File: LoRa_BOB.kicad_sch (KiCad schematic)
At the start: 14 parts, among them U1 1597-1488-ND, U2 XC6210B332MR-G, U3 74HC4050D

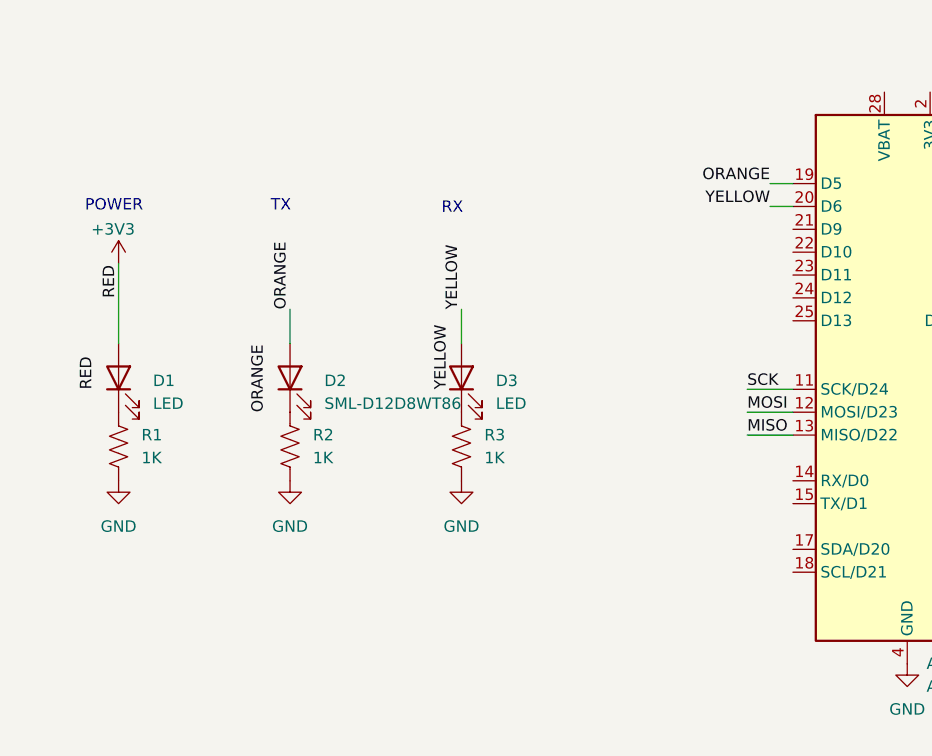
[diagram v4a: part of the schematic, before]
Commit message: better LEDs
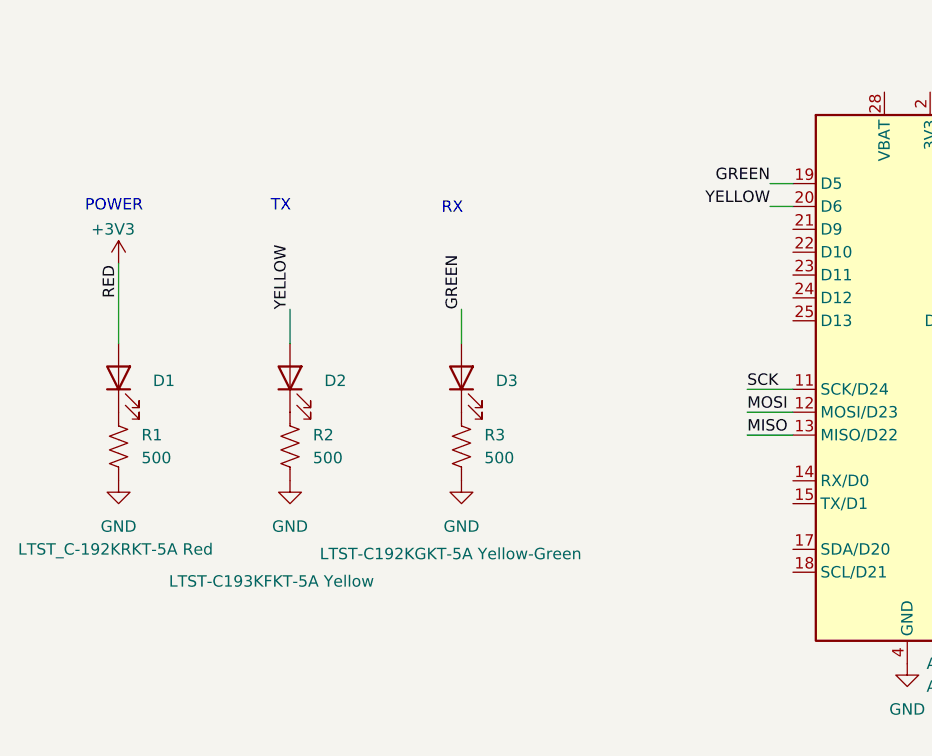
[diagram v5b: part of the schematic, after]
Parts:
- D1: value LED -> LTST_C-192KRKT-5A Red
- D2: value SML-D12D8WT86 -> LTST-C193KFKT-5A Yellow
- D3: value LED -> LTST-C192KGKT-5A Yellow-Green
- R1, R2, R3: value 1K -> 500
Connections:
- net YELLOW: now also D2.2 (A); no longer D3.2 (A)
- net ORANGE renamed GREEN
- net GREEN: now also D3.2 (A); no longer D2.2 (A)
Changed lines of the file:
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@@
 		)
 	)
-	(label "RED"
-		(at 81.28 124.46 90)
-		(effects
-			(font
-				(size 1.27 1.27)
-			)
-			(justify left bottom)
-		)
-	)
-	(label "YELLOW"
+	(label "GREEN"
 		(at 121.92 115.57 90)
 		(effects
@@
 		)
 	)
-	(label "ORANGE"
+	(label "YELLOW"
 		(at 102.87 115.57 90)
 		(effects
@@
 		)
 	)
-	(label "ORANGE"
+	(label "GREEN"
 		(at 156.21 101.6 180)
 		(effects
@@
 		)
 	)
-	(label "YELLOW"
-		(at 120.65 124.46 90)
-		(effects
-			(font
-				(size 1.27 1.27)
-			)
-			(justify left bottom)
-		)
-	)
 	(label "MISO"
 		(at 323.85 166.37 0)
@@
 	(label "SCK_3V"
 		(at 240.03 129.54 0)
-		(effects
-			(font
-				(size 1.27 1.27)
-			)
-			(justify left bottom)
-		)
-	)
-	(label "ORANGE"
-		(at 100.33 127 90)
 		(effects
 			(font
@@
 			)
 		)
-		(property "Value" "1K"
+		(property "Value" "500"
 			(at 105.41 132.0799 0)
 			(effects
@@
 		(on_board yes)
 		(dnp no)
-		(fields_autoplaced yes)
 		(property "Reference" "D3"
 			(at 125.73 123.5074 90)
@@
 			)
 		)
-		(property "Value" "LED"
-			(at 125.73 126.0474 90)
+		(property "Value" "LTST-C192KGKT-5A Yellow-Green"
+			(at 106.172 142.748 90)
 			(effects
 				(font
@@
 			)
 		)
-		(property "Datasheet" "~"
+		(property "Datasheet" "https://www.mouser.com/catalog/specsheets/LTST-C193_Series.pdf"
 			(at 121.92 123.19 0)
 			(effects
@@
 		(on_board yes)
 		(dnp no)
-		(fields_autoplaced yes)
 		(property "Reference" "D1"
 			(at 87.63 123.5074 90)
@@
 			)
 		)
-		(property "Value" "LED"
-			(at 87.63 126.0474 90)
+		(property "Value" "LTST_C-192KRKT-5A Red"
+			(at 72.644 142.24 90)
 			(effects
 				(font
@@
 			)
 		)
-		(property "Datasheet" "~"
+		(property "Datasheet" "https://www.mouser.com/catalog/specsheets/LTST-C193_Series.pdf"
 			(at 83.82 123.19 0)
 			(effects
@@
 		(on_board yes)
 		(dnp no)
-		(fields_autoplaced yes)
 		(property "Reference" "D2"
 			(at 106.68 123.5074 90)
@@
 			)
 		)
-		(property "Value" "SML-D12D8WT86"
-			(at 106.68 126.0474 90)
+		(property "Value" "LTST-C193KFKT-5A Yellow"
+			(at 89.408 145.796 90)
 			(effects
 				(font
@@
 			)
 		)
-		(property "Datasheet" "https://www.rohm.com/datasheet?p=SML-D12D8W&dist=Digi-key&media=referral&source=digi-key.com&campaign=Digi-key"
+		(property "Datasheet" "https://www.mouser.com/catalog/specsheets/LTST-C193_Series.pdf"
 			(at 102.87 123.19 0)
 			(effects
@@
 			)
 		)
-		(property "Value" "1K"
+		(property "Value" "500"
 			(at 86.36 132.0799 0)
 			(effects
@@
 			)
 		)
-		(property "Value" "1K"
+		(property "Value" "500"
 			(at 124.46 132.0799 0)
 			(effects

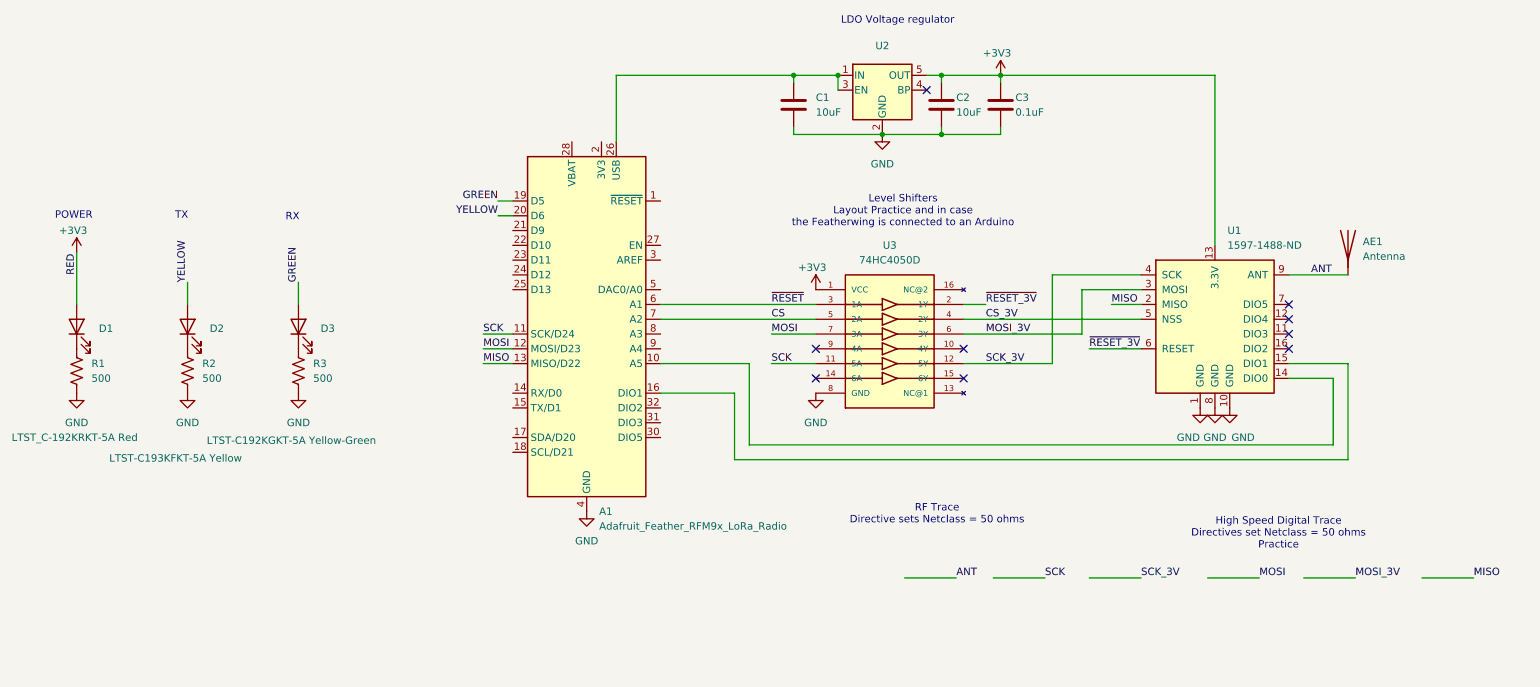
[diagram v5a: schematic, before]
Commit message: Power Flags
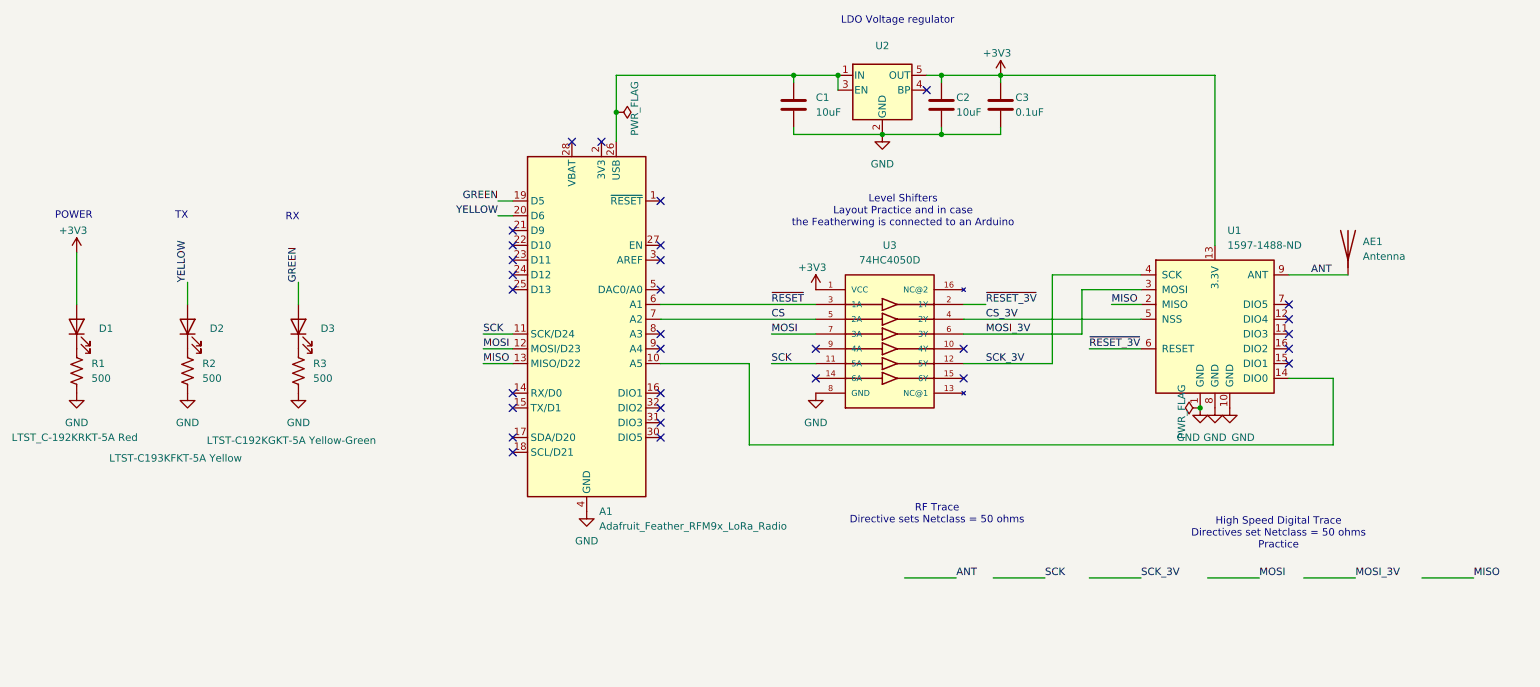
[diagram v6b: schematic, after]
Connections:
- net at A1.16 (DIO1): no longer U1.15 (DIO1)
- no-connect marks 9 -> 31
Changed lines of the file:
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@@
+	)
+	(junction
+		(at 176.53 86.36)
+		(diameter 0)
+		(color 0 0 0 0)
 	)
 	(junction
@@
 		(color 0 0 0 0)
 	)
+	(junction
+		(at 276.86 137.16)
+		(diameter 0)
+		(color 0 0 0 0)
+	)
+	(no_connect
+		(at 184.15 101.6)
+	)
 	(no_connect
 		(at 292.1 127)
 	)
 	(no_connect
+		(at 184.15 111.76)
+	)
+	(no_connect
+		(at 158.75 144.78)
+	)
+	(no_connect
+		(at 184.15 134.62)
+	)
+	(no_connect
+		(at 184.15 139.7)
+	)
+	(no_connect
 		(at 292.1 124.46)
 	)
@@
 	)
 	(no_connect
+		(at 158.75 111.76)
+	)
+	(no_connect
+		(at 168.91 91.44)
+	)
+	(no_connect
+		(at 173.99 91.44)
+	)
+	(no_connect
+		(at 184.15 116.84)
+	)
+	(no_connect
 		(at 229.87 82.55)
 	)
 	(no_connect
+		(at 158.75 114.3)
+	)
+	(no_connect
+		(at 158.75 137.16)
+	)
+	(no_connect
+		(at 158.75 142.24)
+	)
+	(no_connect
+		(at 158.75 116.84)
+	)
+	(no_connect
+		(at 184.15 127)
+	)
+	(no_connect
+		(at 184.15 142.24)
+	)
+	(no_connect
+		(at 158.75 106.68)
+	)
+	(no_connect
+		(at 184.15 124.46)
+	)
+	(no_connect
+		(at 184.15 137.16)
+	)
+	(no_connect
 		(at 236.22 132.08)
 	)
 	(no_connect
+		(at 158.75 134.62)
+	)
+	(no_connect
+		(at 158.75 109.22)
+	)
+	(no_connect
 		(at 210.82 132.08)
 	)
 	(no_connect
+		(at 292.1 129.54)
+	)
+	(no_connect
+		(at 184.15 109.22)
+	)
+	(no_connect
 		(at 236.22 127)
 	)
@@
 	(wire
 		(pts
+			(xy 176.53 86.36) (xy 176.53 80.01)
+		)
+		(stroke
+			(width 0)
+			(type default)
+		)
+	)
+	(wire
+		(pts
 			(xy 256.54 116.84) (xy 266.7 116.84)
 		)
@@
 	(wire
 		(pts
-			(xy 302.26 129.54) (xy 302.26 146.05)
-		)
-		(stroke
-			(width 0)
-			(type default)
-		)
-	)
-	(wire
-		(pts
 			(xy 232.41 80.01) (xy 232.41 81.28)
 		)
@@
 	(wire
 		(pts
-			(xy 196.85 146.05) (xy 302.26 146.05)
-		)
-		(stroke
-			(width 0)
-			(type default)
-		)
-	)
-	(wire
-		(pts
 			(xy 236.22 124.46) (xy 256.54 124.46)
 		)
@@
 	(wire
 		(pts
-			(xy 292.1 129.54) (xy 302.26 129.54)
-		)
-		(stroke
-			(width 0)
-			(type default)
-		)
-	)
-	(wire
-		(pts
 			(xy 153.67 129.54) (xy 158.75 129.54)
 		)
@@
 	(wire
 		(pts
-			(xy 176.53 91.44) (xy 176.53 80.01)
+			(xy 176.53 91.44) (xy 176.53 86.36)
 		)
 		(stroke
@@
 	(wire
 		(pts
-			(xy 184.15 134.62) (xy 196.85 134.62)
-		)
-		(stroke
-			(width 0)
-			(type default)
-		)
-	)
-	(wire
-		(pts
 			(xy 242.57 80.01) (xy 242.57 81.28)
-		)
-		(stroke
-			(width 0)
-			(type default)
-		)
-	)
-	(wire
-		(pts
-			(xy 196.85 134.62) (xy 196.85 146.05)
 		)
 		(stroke
@@
 		)
 	)
-	(label "RED"
-		(at 83.82 114.3 90)
-		(effects
-			(font
-				(size 1.27 1.27)
-			)
-			(justify left bottom)
-		)
-	)
 	(label "SCK_3V"
 		(at 266.7 166.37 0)
@@
 	)
 	(symbol
+		(lib_id "power:PWR_FLAG")
+		(at 176.53 86.36 270)
+		(unit 1)
+		(exclude_from_sim no)
+		(in_bom yes)
+		(on_board yes)
+		(dnp no)
+		(property "Reference" "#FLG02"
+			(at 178.435 86.36 0)
+			(effects
+				(font
+					(size 1.27 1.27)
+				)
+				(hide yes)
+			)
+		)
+		(property "Value" "PWR_FLAG"
+			(at 179.705 81.026 0)
+			(effects
+				(font
+					(size 1.27 1.27)
+				)
+				(justify left)
+			)
+		)
+		(property "Footprint" ""
+			(at 176.53 86.36 0)
+			(effects
+				(font
+					(size 1.27 1.27)
+				)
+				(hide yes)
+			)
+		)
+		(property "Datasheet" "~"
+			(at 176.53 86.36 0)
+			(effects
+				(font
+					(size 1.27 1.27)
+				)
+				(hide yes)
+			)
+		)
+		(property "Description" ""
+			(at 176.53 86.36 0)
+			(effects
+				(font
+					(size 1.27 1.27)
+				)
+				(hide yes)
+			)
+		)
+		(pin "1"
+		)
+		(instances
+			(project "LoRa_BOB"
+				(path "/bd24c4db-4e36-4117-bd4f-5228ef241da9"
+					(reference "#FLG02")
+					(unit 1)
+				)
+			)
+		)
+	)
+	(symbol
 		(lib_id "Regulator_Linear:MIC5205-3.3YM5")
 		(at 222.25 82.55 0)
@@
 					(unit 1)
 				)
+			)
+		)
+	)
+	(symbol
+		(lib_id "power:PWR_FLAG")
+		(at 276.86 137.16 90)
+		(unit 1)
+		(exclude_from_sim no)
+		(in_bom yes)
+		(on_board yes)
+		(dnp no)
+		(property "Reference" "#FLG01"
+			(at 274.955 137.16 0)
+			(effects
+				(font
+					(size 1.27 1.27)
+				)
+				(hide yes)
+			)
+		)
+		(property "Value" "PWR_FLAG"
+			(at 273.685 142.494 0)
+			(effects
+				(font
+					(size 1.27 1.27)
+				)
+				(justify left)
+			)
+		)
+		(property "Footprint" ""
+			(at 276.86 137.16 0)
+			(effects
+				(font
+					(size 1.27 1.27)
+				)
+				(hide yes)
+			)
+		)
+		(property "Datasheet" "~"
+			(at 276.86 137.16 0)
+			(effects
+				(font
+					(size 1.27 1.27)
+				)
+				(hide yes)
+			)
+		)
+		(property "Description" ""
+			(at 276.86 137.16 0)
+			(effects
+				(font
+					(size 1.27 1.27)
+				)
+				(hide yes)
+			)
+		)
+		(pin "1"
+		)
+		(instances
+			(project "LoRa_BOB"
+				(path "/bd24c4db-4e36-4117-bd4f-5228ef241da9"
+					(reference "#FLG01")
+					(unit 1)
+				)

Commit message: R's are 0603
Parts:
- R1, R2, R3: footprint Resistor_SMD:R_0201_0603Metric_Pad0.64x0.40mm_HandSolder -> Resistor_SMD:R_0603_1608Metric_Pad0.98x0.95mm_HandSolder
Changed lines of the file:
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@@
 			)
 		)
-		(property "Footprint" "Resistor_SMD:R_0201_0603Metric_Pad0.64x0.40mm_HandSolder"
+		(property "Footprint" "Resistor_SMD:R_0603_1608Metric_Pad0.98x0.95mm_HandSolder"
 			(at 103.886 131.064 90)
 			(effects
@@
 			)
 		)
-		(property "Footprint" "Resistor_SMD:R_0201_0603Metric_Pad0.64x0.40mm_HandSolder"
+		(property "Footprint" "Resistor_SMD:R_0603_1608Metric_Pad0.98x0.95mm_HandSolder"
 			(at 84.836 131.064 90)
 			(effects
@@
 			)
 		)
-		(property "Footprint" "Resistor_SMD:R_0201_0603Metric_Pad0.64x0.40mm_HandSolder"
+		(property "Footprint" "Resistor_SMD:R_0603_1608Metric_Pad0.98x0.95mm_HandSolder"
 			(at 122.936 131.064 90)
 			(effects

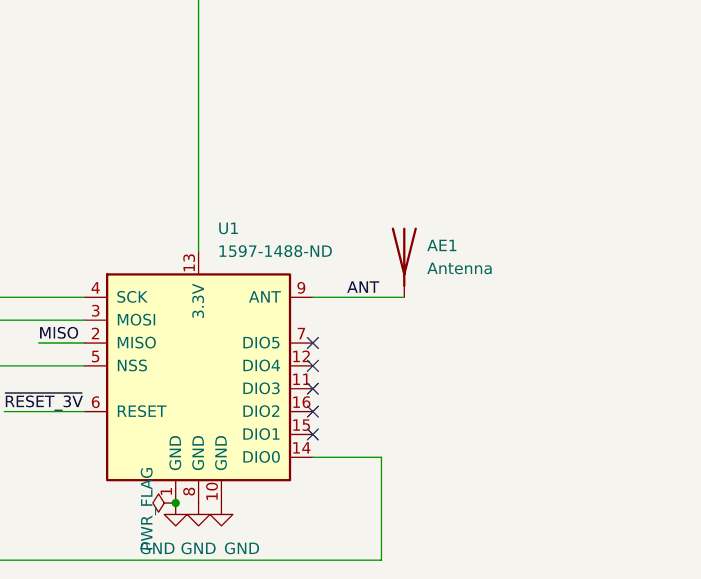
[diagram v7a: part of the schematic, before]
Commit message: Added Antenna Matching L and C
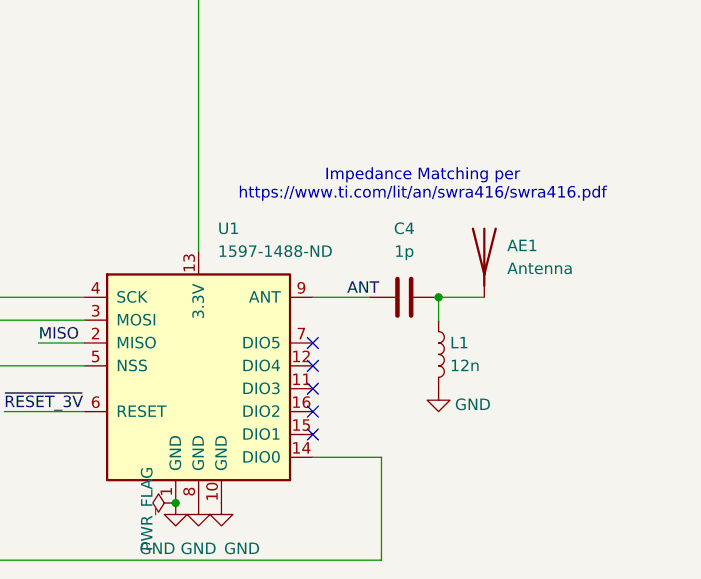
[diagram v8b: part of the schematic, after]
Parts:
- added C4: 1p, Capacitor_SMD:C_0603_1608Metric_Pad1.08x0.95mm_HandSolder, symbol Device:C
- added L1: 12n, Inductor_SMD:L_0603_1608Metric_Pad1.05x0.95mm_HandSolder, symbol Device:L
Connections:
- net ANT: now also C4.1; no longer AE1.1 (A)
- net GND: now also L1.2
- new net: AE1.1 (A), C4.2, L1.1
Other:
- note added: "Impedance Matching per https://www.ti.com/lit/an/swra416/swra416.pdf"
- moved on the sheet: AE1
